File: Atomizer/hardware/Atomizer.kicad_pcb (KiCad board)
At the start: 2 copper layers, 54.6 x 98.6 mm, 49 parts

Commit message: atomizer schematic graphics update
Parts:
- SW_MODE1: footprint TE_Alcoswitch_Tactile_2-1825910-7:SW_2-1825910-7 -> TE_1-1825910-4:SW_2-1825910-7
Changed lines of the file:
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@@
-(kicad_pcb (version 20171130) (host pcbnew "(5.0.0-3-g5ebb6b6)")
+(kicad_pcb (version 20171130) (host pcbnew "(5.0.0)")
   (general
     (thickness 1.6)
@@
   )
   (layers
-    (0 F.Cu signal)
-    (31 B.Cu signal)
-    (32 B.Adhes user)
-    (33 F.Adhes user)
-    (34 B.Paste user)
-    (35 F.Paste user)
-    (36 B.SilkS user)
-    (37 F.SilkS user)
-    (38 B.Mask user)
-    (39 F.Mask user)
+    (0 F.Cu signal hide)
+    (31 B.Cu signal hide)
+    (32 B.Adhes user hide)
+    (33 F.Adhes user hide)
+    (34 B.Paste user hide)
+    (35 F.Paste user hide)
+    (36 B.SilkS user hide)
+    (37 F.SilkS user hide)
+    (38 B.Mask user hide)
+    (39 F.Mask user hide)
     (40 Dwgs.User user)
-    (41 Cmts.User user)
-    (42 Eco1.User user)
-    (43 Eco2.User user)
+    (41 Cmts.User user hide)
+    (42 Eco1.User user hide)
+    (43 Eco2.User user hide)
     (44 Edge.Cuts user)
-    (45 Margin user)
+    (45 Margin user hide)
     (46 B.CrtYd user hide)
     (47 F.CrtYd user hide)
     (48 B.Fab user hide)
-    (49 F.Fab user hide)
+    (49 F.Fab user)
   )
   (setup
@@
     (add_net "Net-(R_MODE1-Pad2)")
   )
-  (module TE_Alcoswitch_Tactile_2-1825910-7:SW_2-1825910-7 (layer F.Cu)
+  (module TE_1-1825910-4:SW_2-1825910-7 (layer F.Cu)
     (at 80.7085 90.8685)
     (fp_text reference SW_MODE1 (at -2.98289 -3.90753) (layer F.SilkS)
@@
       (effects (font (size 0.480673 0.480673) (thickness 0.05)))
     )
+    (fp_circle (center 0 0) (end 1.5 0) (layer Dwgs.User) (width 0.2))
+    (fp_line (start -2.995 2.995) (end -2.995 -2.995) (layer Dwgs.User) (width 0.127))
+    (fp_line (start -2.995 -2.995) (end 2.995 -2.995) (layer Dwgs.User) (width 0.127))
+    (fp_line (start 2.995 -2.995) (end 2.995 2.995) (layer Dwgs.User) (width 0.127))
+    (fp_line (start 2.995 2.995) (end -2.995 2.995) (layer Dwgs.User) (width 0.127))
+    (fp_line (start -2.995 -1.12) (end -2.995 1.15) (layer F.SilkS) (width 0.127))
+    (fp_line (start -2.13 -2.995) (end 2.37 -2.995) (layer F.SilkS) (width 0.127))
+    (fp_line (start 2.995 -1.15) (end 2.995 1.15) (layer F.SilkS) (width 0.127))
+    (fp_line (start -2.4 3) (end 2.4 3) (layer F.SilkS) (width 0.127))
+    (fp_line (start -4.25 3.25) (end -4.25 -3.25) (layer Eco1.User) (width 0.05))
+    (fp_line (start -4.25 -3.25) (end 4.25 -3.25) (layer Eco1.User) (width 0.05))
+    (fp_line (start 4.25 -3.25) (end 4.25 3.25) (layer Eco1.User) (width 0.05))
+    (fp_line (start 4.25 3.25) (end -4.25 3.25) (layer Eco1.User) (width 0.05))
+    (fp_circle (center -2.379 -2.3) (end -2.279 -2.3) (layer Dwgs.User) (width 0.3))
     (fp_circle (center -4.778 -2.132) (end -4.678 -2.132) (layer F.SilkS) (width 0.3))
-    (fp_circle (center -2.379 -2.3) (end -2.279 -2.3) (layer Dwgs.User) (width 0.3))
-    (fp_line (start 4.25 3.25) (end -4.25 3.25) (layer Eco1.User) (width 0.05))
-    (fp_line (start 4.25 -3.25) (end 4.25 3.25) (layer Eco1.User) (width 0.05))
-    (fp_line (start -4.25 -3.25) (end 4.25 -3.25) (layer Eco1.User) (width 0.05))
-    (fp_line (start -4.25 3.25) (end -4.25 -3.25) (layer Eco1.User) (width 0.05))
-    (fp_line (start -2.4 3) (end 2.4 3) (layer F.SilkS) (width 0.127))
-    (fp_line (start 2.995 -1.15) (end 2.995 1.15) (layer F.SilkS) (width 0.127))
-    (fp_line (start -2.13 -2.995) (end 2.37 -2.995) (layer F.SilkS) (width 0.127))
-    (fp_line (start -2.995 -1.12) (end -2.995 1.15) (layer F.SilkS) (width 0.127))
-    (fp_line (start 2.995 2.995) (end -2.995 2.995) (layer Dwgs.User) (width 0.127))
-    (fp_line (start 2.995 -2.995) (end 2.995 2.995) (layer Dwgs.User) (width 0.127))
-    (fp_line (start -2.995 -2.995) (end 2.995 -2.995) (layer Dwgs.User) (width 0.127))
-    (fp_line (start -2.995 2.995) (end -2.995 -2.995) (layer Dwgs.User) (width 0.127))
-    (pad 3 thru_hole circle (at 3.25 -2.25) (size 1.498 1.498) (drill 0.99) (layers *.Cu *.Mask)
-      (net 20 /GND))
-    (pad 4 thru_hole circle (at 3.25 2.25) (size 1.498 1.498) (drill 0.99) (layers *.Cu *.Mask))
+    (pad 1 thru_hole rect (at -3.25 -2.25) (size 1.498 1.498) (drill 0.99) (layers *.Cu *.Mask))
     (pad 2 thru_hole circle (at -3.25 2.25) (size 1.498 1.498) (drill 0.99) (layers *.Cu *.Mask)
       (net 38 "Net-(R_MODE1-Pad2)"))
-    (pad 1 thru_hole rect (at -3.25 -2.25) (size 1.498 1.498) (drill 0.99) (layers *.Cu *.Mask))
+    (pad 4 thru_hole circle (at 3.25 2.25) (size 1.498 1.498) (drill 0.99) (layers *.Cu *.Mask))
+    (pad 3 thru_hole circle (at 3.25 -2.25) (size 1.498 1.498) (drill 0.99) (layers *.Cu *.Mask)
+      (net 20 /GND))
     (model ${KIPRJMOD}/LIBS/3D/c-2-1825910-7-c-3d.stp
       (offset (xyz 0 0 13))
       (scale (xyz 1 1 1))
       (rotate (xyz 0 0 -90))
+    )
+  )
+  (module custom_sw:SW_3PDT_W18MM_L17.3MM_P5.3MM_D2MM (layer F.Cu)
+    (at 80.5434 160.0327 180)
+    (fp_text reference SW_EN1 (at 7.3914 9.1567 180) (layer F.SilkS)
+      (effects (font (size 0.5 0.5) (thickness 0.125)))
+    )
+    (fp_text value SW_3PDT_on_on (at 0.254 14.478 180) (layer F.Fab)
+      (effects (font (size 0.5 0.5) (thickness 0.125)))
+    )
+    (fp_line (start -8.89 -8.509) (end 7.62 -8.509) (layer F.SilkS) (width 0.15))
+    (fp_line (start 7.62 -8.509) (end 8.89 -8.509) (layer F.SilkS) (width 0.15))
+    (fp_line (start 9.017 -8.89) (end 9.017 8.89) (layer F.SilkS) (width 0.15))
+    (fp_line (start 8.89 8.509) (end -8.89 8.509) (layer F.SilkS) (width 0.15))
+    (fp_line (start -9.017 8.89) (end -9.017 -8.89) (layer F.SilkS) (width 0.15))
+    (fp_circle (center 0 0) (end 5.5 0) (layer Dwgs.User) (width 0.5))
+    (pad 1 thru_hole oval (at -5.29336 -4.81838 180) (size 3.5 3) (drill 1.5) (layers *.Cu *.Mask)
+      (net 31 /Atomizer_3PDT/3PDT_1_INT))
+    (pad 4 thru_hole oval (at -0.02032 -4.80568 180) (size 3.5 3) (drill 1.5) (layers *.Cu *.Mask)
+      (net 28 /Atomizer_3PDT/3PDT_4_INT))
+    (pad 7 thru_hole oval (at 5.2959 -4.8006 180) (size 3.5 3) (drill 1.5) (layers *.Cu *.Mask)
+      (net 25 /Atomizer_3PDT/3PDT_7_INT))
+    (pad 2 thru_hole oval (at -5.3086 -0.0127 180) (size 3.5 3) (drill 1.5) (layers *.Cu *.Mask)
+      (net 30 /Atomizer_3PDT/3PDT_2_INT))
+    (pad 5 thru_hole oval (at -0.0127 -0.0127 180) (size 3.5 3) (drill 1.5) (layers *.Cu *.Mask)
+      (net 27 /Atomizer_3PDT/3PDT_5_INT))
+    (pad 8 thru_hole oval (at 5.2959 -0.0127 180) (size 3.5 3) (drill 1.5) (layers *.Cu *.Mask)
+      (net 24 /Atomizer_3PDT/3PDT_8_INT))
+    (pad 3 thru_hole oval (at -5.3213 4.7879 180) (size 3.5 3) (drill 1.5) (layers *.Cu *.Mask)
+      (net 29 /Atomizer_3PDT/3PDT_3_INT))
+    (pad 6 thru_hole oval (at -0.0127 4.7879 180) (size 3.5 3) (drill 1.5) (layers *.Cu *.Mask)
+      (net 26 /Atomizer_3PDT/3PDT_6_INT))
+    (pad 9 thru_hole oval (at 5.2959 4.7879 180) (size 3.5 3) (drill 1.5) (layers *.Cu *.Mask)
+      (net 23 /Atomizer_3PDT/3PDT_9_INT))
+    (model "${KIPRJMOD}/LIBS/3D/3PDT Switch/3PDT.stp"
+      (offset (xyz -9 -6.25 0))
+      (scale (xyz 1 1 1))
+      (rotate (xyz 0 0 0))
     )
   )
@@
       (scale (xyz 1 1 1))
       (rotate (xyz 0 0 0))
-    )
-  )
-  (module custom_sw:SW_3PDT_W18MM_L17.3MM_P5.3MM_D2MM (layer F.Cu)
-    (at 80.5434 160.0327 180)
-    (fp_text reference SW_EN1 (at 7.3914 9.1567 180) (layer F.SilkS)
-      (effects (font (size 0.5 0.5) (thickness 0.125)))
-    )
-    (fp_text value SW_3PDT_on_on (at 0.254 14.478 180) (layer F.Fab)
-      (effects (font (size 0.5 0.5) (thickness 0.125)))
-    )
-    (fp_line (start -8.89 -8.509) (end 7.62 -8.509) (layer F.SilkS) (width 0.15))
-    (fp_line (start 7.62 -8.509) (end 8.89 -8.509) (layer F.SilkS) (width 0.15))
-    (fp_line (start 9.017 -8.89) (end 9.017 8.89) (layer F.SilkS) (width 0.15))
-    (fp_line (start 8.89 8.509) (end -8.89 8.509) (layer F.SilkS) (width 0.15))
-    (fp_line (start -9.017 8.89) (end -9.017 -8.89) (layer F.SilkS) (width 0.15))
-    (pad 1 thru_hole oval (at -5.29336 -4.81838 180) (size 3.5 3) (drill 1.5) (layers *.Cu *.Mask)
-      (net 31 /Atomizer_3PDT/3PDT_1_INT))
-    (pad 4 thru_hole oval (at -0.02032 -4.80568 180) (size 3.5 3) (drill 1.5) (layers *.Cu *.Mask)
-      (net 28 /Atomizer_3PDT/3PDT_4_INT))
-    (pad 7 thru_hole oval (at 5.2959 -4.8006 180) (size 3.5 3) (drill 1.5) (layers *.Cu *.Mask)
-      (net 25 /Atomizer_3PDT/3PDT_7_INT))
-    (pad 2 thru_hole oval (at -5.3086 -0.0127 180) (size 3.5 3) (drill 1.5) (layers *.Cu *.Mask)
-      (net 30 /Atomizer_3PDT/3PDT_2_INT))
-    (pad 5 thru_hole oval (at -0.0127 -0.0127 180) (size 3.5 3) (drill 1.5) (layers *.Cu *.Mask)
-      (net 27 /Atomizer_3PDT/3PDT_5_INT))
-    (pad 8 thru_hole oval (at 5.2959 -0.0127 180) (size 3.5 3) (drill 1.5) (layers *.Cu *.Mask)
-      (net 24 /Atomizer_3PDT/3PDT_8_INT))
-    (pad 3 thru_hole oval (at -5.3213 4.7879 180) (size 3.5 3) (drill 1.5) (layers *.Cu *.Mask)
-      (net 29 /Atomizer_3PDT/3PDT_3_INT))
-    (pad 6 thru_hole oval (at -0.0127 4.7879 180) (size 3.5 3) (drill 1.5) (layers *.Cu *.Mask)
-      (net 26 /Atomizer_3PDT/3PDT_6_INT))
-    (pad 9 thru_hole oval (at 5.2959 4.7879 180) (size 3.5 3) (drill 1.5) (layers *.Cu *.Mask)
-      (net 23 /Atomizer_3PDT/3PDT_9_INT))
-    (model "${KIPRJMOD}/LIBS/3D/3PDT Switch/3PDT.stp"
-      (offset (xyz -9 -6.25 0))
-      (scale (xyz 1 1 1))
-      (rotate (xyz 0 0 0))

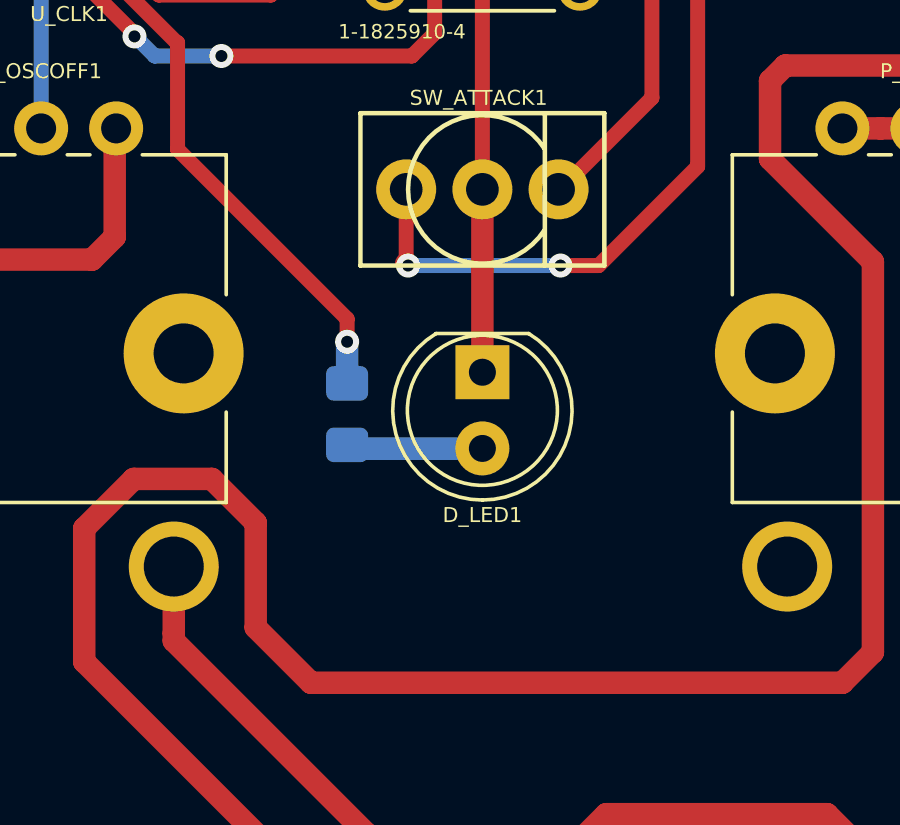
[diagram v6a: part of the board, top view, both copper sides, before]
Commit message: Updated BOM. Converted to Mouser list. Moved LED away from switch
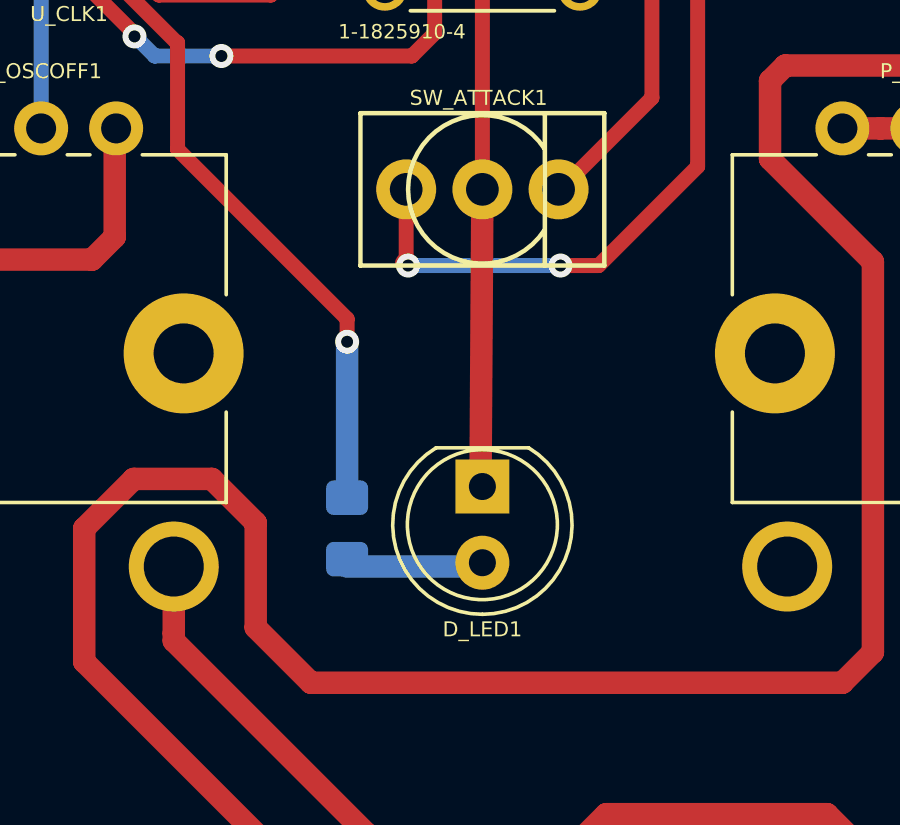
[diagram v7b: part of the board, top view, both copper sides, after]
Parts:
- moved R_LPF1 3.81 mm to (76.2, 111.1)
- moved D_LED1 3.81 mm to (80.7, 109.7)
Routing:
- net Net-(D_LED1-Pad1): track 26.8 -> 31.0 mm
- net /Atomizer_Clock/CLK_OUT_PIN: track 30.6 -> 34.1 mm
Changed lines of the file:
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@@
-(kicad_pcb (version 20171130) (host pcbnew "(5.0.0)")
+(kicad_pcb (version 20171130) (host pcbnew "(5.0.0-3-g5ebb6b6)")
   (general
     (thickness 1.6)
     (drawings 30)
-    (tracks 451)
+    (tracks 448)
     (zones 0)
     (modules 49)
@@
   )
   (layers
-    (0 F.Cu signal hide)
-    (31 B.Cu signal hide)
-    (32 B.Adhes user hide)
-    (33 F.Adhes user hide)
-    (34 B.Paste user hide)
-    (35 F.Paste user hide)
-    (36 B.SilkS user hide)
-    (37 F.SilkS user hide)
-    (38 B.Mask user hide)
-    (39 F.Mask user hide)
+    (0 F.Cu signal)
+    (31 B.Cu signal)
+    (32 B.Adhes user)
+    (33 F.Adhes user)
+    (34 B.Paste user)
+    (35 F.Paste user)
+    (36 B.SilkS user)
+    (37 F.SilkS user)
+    (38 B.Mask user)
+    (39 F.Mask user)
     (40 Dwgs.User user)
-    (41 Cmts.User user hide)
-    (42 Eco1.User user hide)
-    (43 Eco2.User user hide)
+    (41 Cmts.User user)
+    (42 Eco1.User user)
+    (43 Eco2.User user)
     (44 Edge.Cuts user)
-    (45 Margin user hide)
-    (46 B.CrtYd user hide)
-    (47 F.CrtYd user hide)
-    (48 B.Fab user hide)
+    (45 Margin user)
+    (46 B.CrtYd user)
+    (47 F.CrtYd user)
+    (48 B.Fab user)
     (49 F.Fab user)
   )
@@
       (drillshape 0)
       (scaleselection 1)
-      (outputdirectory "../docs/GERBERS/"))
+      (outputdirectory "../docs/ATOMIZER_REVA/"))
   )
   (net 0 "")
@@
   )
   (module Resistor_SMD:R_0805_2012Metric_Pad1.15x1.40mm_HandSolder (layer B.Cu)
-    (at 76.2 107.315 90)
+    (at 76.2 111.125 90)
     (descr "Resistor SMD 0805 (2012 Metric), square (rectangular) end terminal, IPC_7351 nominal with elongated pad for handsoldering. (Body size source: https://docs.google.com/spreadsheets/d/1BsfQQcO9C6DZCsRaXUlFlo91Tg2WpOkGARC1WS5S8t0/edit?usp=sharing), generated with kicad-footprint-generator")
     (tags "resistor handsolder")
@@
   )
   (module LED_THT:LED_D5.0mm (layer F.Cu)
-    (at 80.708741 105.918 270)
+    (at 80.708741 109.728 270)
     (descr "LED, diameter 5.0mm, 2 pins, http://cdn-reichelt.de/documents/datenblatt/A500/LL-504BC2E-009.pdf")
     (tags "LED diameter 5.0mm 2 pins")
@@
   (segment (start 69.301357 90.7415) (end 66.08 87.520143) (width 0.5) (layer F.Cu) (net 35))
   (segment (start 70.833 90.7415) (end 69.301357 90.7415) (width 0.5) (layer F.Cu) (net 35) (status 10))
-  (segment (start 76.2 106.417) (end 76.2 105.742) (width 0.75) (layer B.Cu) (net 36) (status 30))
   (via (at 76.2 104.902) (size 0.8) (drill 0.4) (layers F.Cu B.Cu) (net 36))
-  (segment (start 76.2 105.742) (end 76.2 104.902) (width 0.75) (layer B.Cu) (net 36) (status 10))
   (segment (start 57.3405 89.197) (end 57.5105 89.027) (width 0.25) (layer B.Cu) (net 36))
   (segment (start 61.98532 89.4715) (end 61.980659 89.466839) (width 0.25) (layer F.Cu) (net 36))
@@
   (segment (start 70.833 92.0115) (end 69.581393 92.0115) (width 0.5) (layer F.Cu) (net 40) (status 10))
   (segment (start 80.772 99.758741) (end 80.708741 99.822) (width 0.75) (layer B.Cu) (net 41) (status 30))
-  (segment (start 80.772 105.664) (end 80.708741 105.600741) (width 0.75) (layer F.Cu) (net 41) (status 30))
-  (segment (start 80.708741 105.600741) (end 80.708741 99.885259) (width 0.75) (layer F.Cu) (net 41) (status 30))
   (segment (start 85.979 86.2965) (end 84.1375 84.455) (width 0.5) (layer F.Cu) (net 41))
   (segment (start 85.979 89.0905) (end 85.979 86.2965) (width 0.5) (layer F.Cu) (net 41))
@@
   (segment (start 80.708741 99.822) (end 80.7085 99.821759) (width 0.5) (layer F.Cu) (net 41))
   (segment (start 84.1375 84.455) (end 82.575 84.455) (width 0.5) (layer F.Cu) (net 41))
-  (segment (start 80.699741 108.467) (end 80.708741 108.458) (width 0.75) (layer B.Cu) (net 42) (status 30))
-  (segment (start 76.2 108.467) (end 80.699741 108.467) (width 0.75) (layer B.Cu) (net 42) (status 30))
+  (segment (start 76.2 109.855) (end 76.2 104.902) (width 0.75) (layer B.Cu) (net 36))
+  (segment (start 80.645 109.855) (end 80.708741 99.885259) (width 0.75) (layer F.Cu) (net 41))
+  (segment (start 76.2 112.395) (end 80.699741 112.395) (width 0.75) (layer B.Cu) (net 42) (status 30))
   (segment (start 75.82 76.834) (end 76.2 76.454) (width 0.75) (layer F.Cu) (net 43) (status 30))
   (segment (start 75.82 77.217) (end 75.819 77.216) (width 0.75) (layer F.Cu) (net 43))

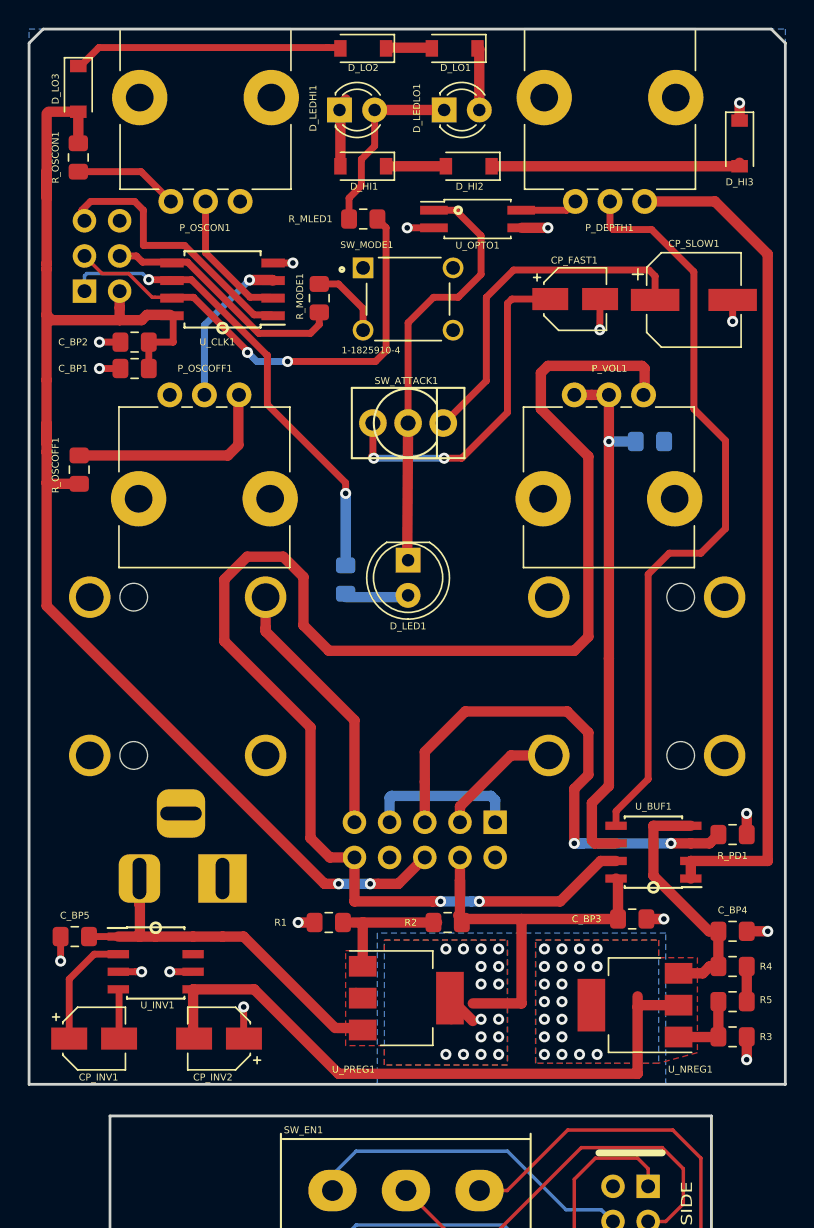
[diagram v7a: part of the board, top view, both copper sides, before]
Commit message: updated atomizer
- changed input pulldown resistor from 22M to 1M
- added output lpf filter (1uF, 100K)
- updated docs
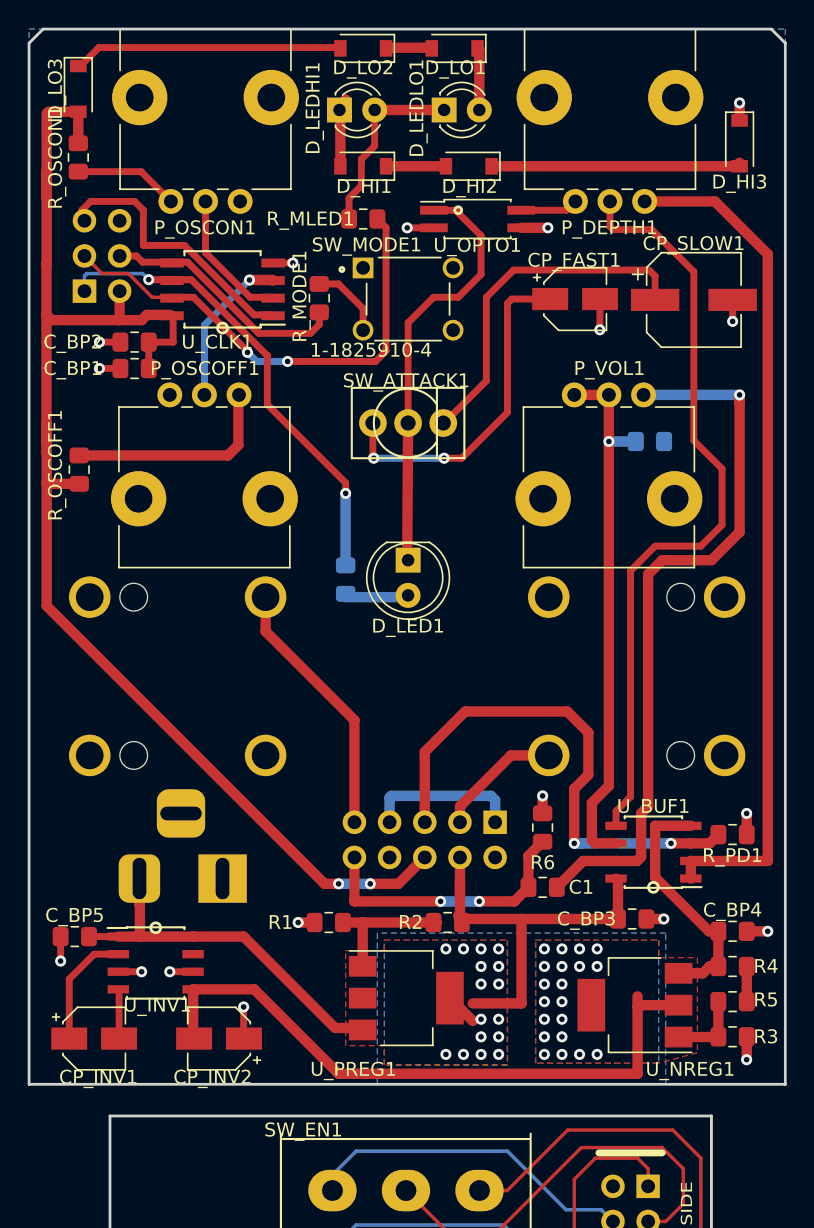
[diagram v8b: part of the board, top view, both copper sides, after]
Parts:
- added C1: 1uF, Capacitor_SMD:C_0805_2012Metric_Pad1.15x1.40mm_HandSolder, F.Cu at (90.4, 133.3)
- added R6: 100K, Resistor_SMD:R_0805_2012Metric_Pad1.15x1.40mm_HandSolder, F.Cu at (90.4, 129.0)
- R_PD1: value 22M -> 1M
- SW_MODE1: footprint TE_1-1825910-4:SW_2-1825910-7 -> TE_Alcoswitch_Tactile_2-1825910-7:SW_2-1825910-7
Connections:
- P_VOL1 pad 3: /3PDT_6_EXT -> Net-(C1-Pad2)
- U_BUF1 pad 7: /3PDT_6_EXT -> Net-(C1-Pad2)
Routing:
- net /3PDT_6_EXT: track 111.3 -> 20.2 mm
- net Net-(C1-Pad2): track 0.00 -> 53.3 mm, vias 0 -> 1
- net /GND: track 28.1 -> 29.4 mm, vias 17 -> 18
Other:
- board text added: "ATOMIZER Chris Sutton RevB 2019"
- board text removed: "ATOMIZER Chris Sutton RevA 2018"
